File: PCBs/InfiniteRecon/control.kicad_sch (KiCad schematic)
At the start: 0 parts

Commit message: Finished Scem for the most part, awake me needs to look it over one more time
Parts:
- added C10, C11, C13, C15, C16: 0.1uF, PCM_JLCPCB:C_0402, symbol PCM_JLCPCB-Capacitors:0402,100nF
- added C12: 1uF, PCM_JLCPCB:C_0603, symbol PCM_JLCPCB-Capacitors:0603,1uF
- added C14: 22uF, PCM_JLCPCB:C_0805, symbol PCM_JLCPCB-Capacitors:0805,22uF
- added D6: WS2812B, LED_SMD:LED_WS2812B_PLCC4_5.0x5.0mm_P3.2mm, symbol LED:WS2812B
- added R14: 20kΩ, PCM_JLCPCB:R_0402, symbol Device:R_Small_US
- added R15, R28, R29, R30, R31: 10K, Resistor_SMD:R_01005_0402Metric, symbol Device:R_Small_US
- added R16: 100K, PCM_JLCPCB:R_0402, symbol Device:R_Small_US
- added R32, R33: 10K, Resistor_SMD:R_0603_1608Metric_Pad0.98x0.95mm_HandSolder, symbol Device:R_Small_US
- added S1: RESET, PCM_JLCPCB:SW-SMD_4P-L5.1-W5.1-P3.70-LS6.5-TL-2, symbol PCM_JLCPCB-Connectors_Buttons:Tactile Button, 160gf, 12V, 50mA, 5.1mm
- added S2: BOOT, PCM_JLCPCB:SW-SMD_4P-L5.1-W5.1-P3.70-LS6.5-TL-2, symbol PCM_JLCPCB-Connectors_Buttons:Tactile Button, 160gf, 12V, 50mA, 5.1mm
- added SIM1: 1040310811, Connector_Card:microSD_HC_Molex_104031-0811, symbol JLCImport:1040310811
- added U6: TPL5010DDCR, Package_TO_SOT_SMD:SOT-23-6, symbol JLCImport:TPL5010DDCR
- added U7: ESP32-S3-WROOM-1, RF_Module:ESP32-S3-WROOM-1, symbol RF_Module:ESP32-S3-WROOM-1
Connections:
- new net: C13.1, S2.2 (B), S2.4 (D), U7.27 (IO0)
- new net: R33.1, SIM1.8 (DAT1)
- new net: R14.2, U6.3 (DELAY/M_RST)
- new net: R32.1, SIM1.1 (DAT2)
- new net 3V3: C10.1, C14.1, C15.1, C16.1, D6.1 (VDD), R15.1, R16.1, R28.1, R29.1, U6.1 (VDD), U7.2 (3V3)
- new net 3V3_SW: R30.1, R31.1, R32.2, R33.2, SIM1.4 (VDD)
- new net 3V3_SW_EN: U7.34 (IO41)
- new net BATT_ALERT: U7.33 (IO40)
- new net CS: SIM1.2 (DAT3/CD), U7.7 (IO7)
- new net GND: C10.2, C11.2, C12.2, C13.2, C14.2, C15.2, C16.2, D6.3 (VSS), R14.1, S1.1 (A), S1.3 (C), S2.1 (A), S2.3 (C), SIM1.6 (VSS), SIM1.SH (SHIELD), U6.2 (GND), U7.1 (GND), U7.40 (GND), U7.41 (GND)
- new net MIC_THSEL: U7.32 (IO39)
- new net MIC_WAKE: U7.31 (IO38)
- new net MISO: SIM1.7 (DAT0), U7.17 (IO9)
- new net MOSI: SIM1.3 (CMD), U7.12 (IO8)
- new net NEOPIXEL: D6.4 (DIN), U7.25 (IO48)
- new net SCK: SIM1.5 (CLK), U7.18 (IO10)
- new net SCL_1: R28.2, U7.5 (IO5)
- new net SCL_SW: R30.2, U7.21 (IO13)
- new net SDA_1: R29.2, U7.4 (IO4)
- new net SDA_SW: R31.2, U7.20 (IO12)
- new net TDM_BCLK: U7.8 (IO15)
- new net TDM_FSYNC: U7.9 (IO16)
- new net TDM_SDOUT: U7.22 (IO14)
- new net USB_D+: U7.14 (USB_D+)
- new net USB_D-: U7.13 (USB_D-)
- new net WD_FEED: U6.4 (DONE), U7.38 (IO2)
- new net WD_RST: C11.1, C12.1, R15.2, R16.2, S1.2 (B), S1.4 (D), U6.6 (RSTn), U7.3 (EN)
- new net WD_WAKE: U6.5 (WAKE), U7.39 (IO1)
- no-connect marks 0 -> 17
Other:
- note added: "20K -> ~47s timer"
- note added: "ESP32S3 N8R8 Wroom-1"
- note added: "I2C Pullups"
- note added: "MicroSd Card"
- note added: "NeoPixel"
- note added: "Watchdog"

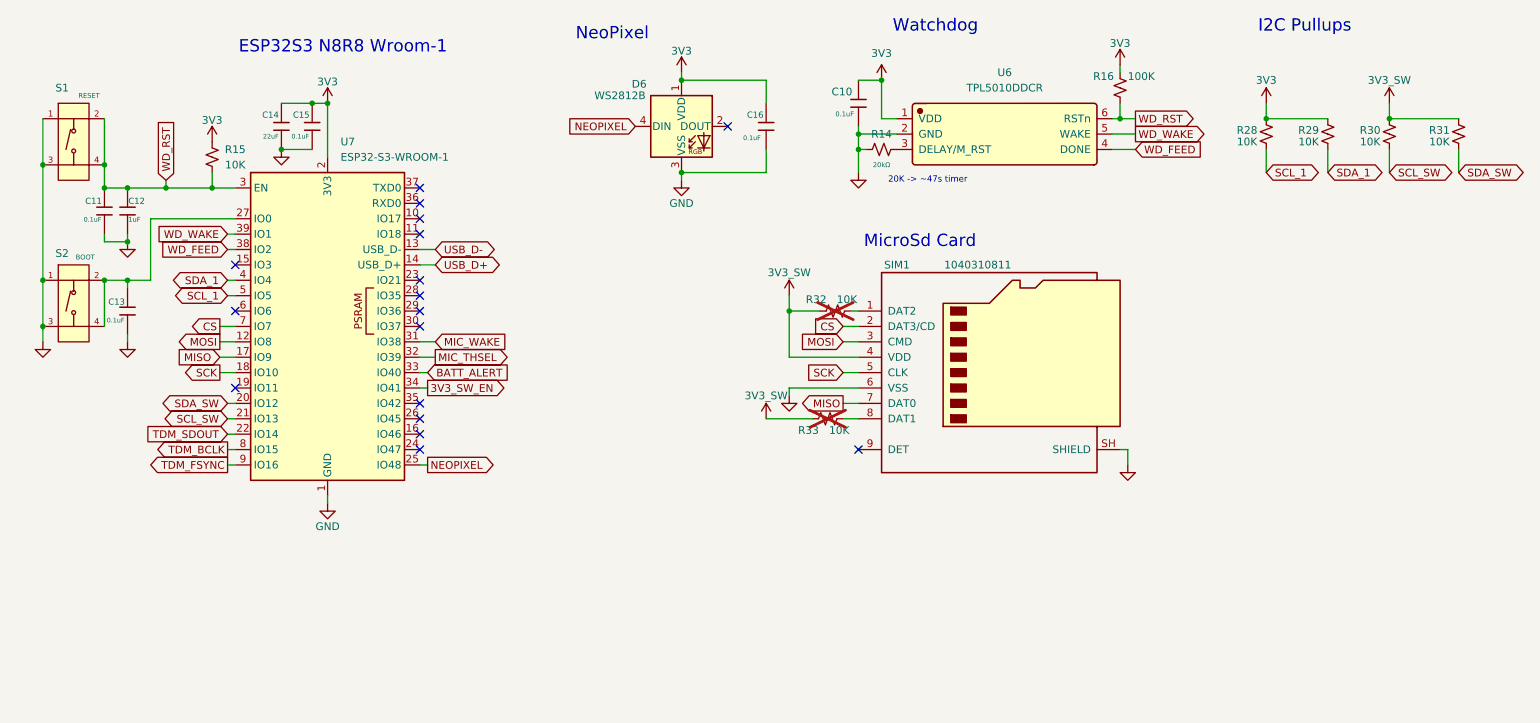
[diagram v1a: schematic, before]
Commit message: Fixed footprints and some not connected caps
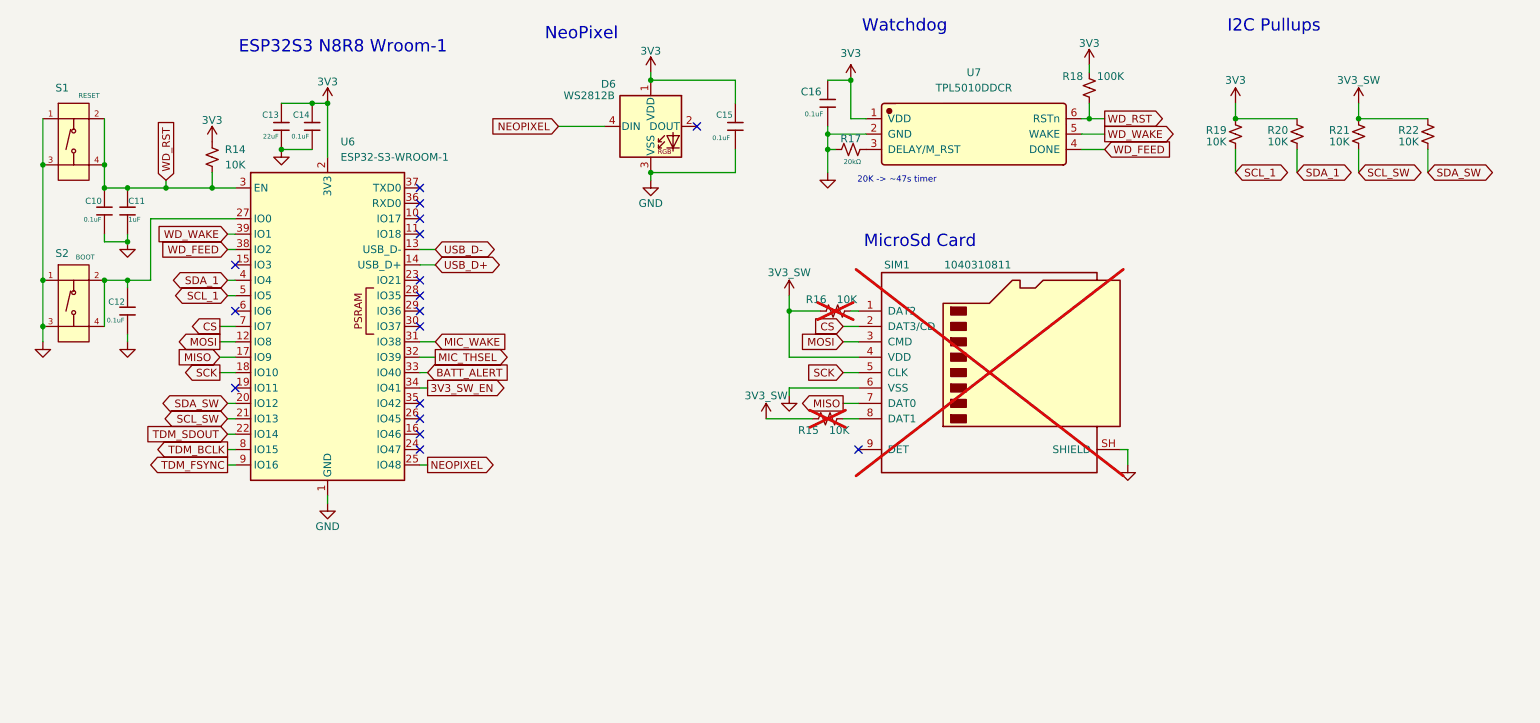
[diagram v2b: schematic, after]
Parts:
- R14: renamed from R15; footprint Resistor_SMD:R_01005_0402Metric -> Resistor_SMD:R_0402_1005Metric
- R19: renamed from R28; footprint Resistor_SMD:R_01005_0402Metric -> Resistor_SMD:R_0402_1005Metric
- R20: renamed from R29; footprint Resistor_SMD:R_01005_0402Metric -> Resistor_SMD:R_0402_1005Metric
- R21: renamed from R30; footprint Resistor_SMD:R_01005_0402Metric -> Resistor_SMD:R_0402_1005Metric
- R22: renamed from R31; footprint Resistor_SMD:R_01005_0402Metric -> Resistor_SMD:R_0402_1005Metric
- SIM1: now not fitted
- renumbered C11 to C10, C12 to C11, C13 to C12, C14 to C13, C15 to C14, C16 to C15, C10 to C16, R33 to R15, R32 to R16, R14 to R17, R16 to R18, U7 to U6, U6 to U7
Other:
- moved on the sheet: C15, C16, D6, R17, R18, R19, R20, R21, R22, U7

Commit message: Finished scem
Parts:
- added R34, R35, R39: 10K, Resistor_SMD:R_0603_1608Metric_Pad0.98x0.95mm_HandSolder, symbol Device:R_Small_US
- added R38: 100K, PCM_JLCPCB:R_0402, symbol Device:R_Small_US
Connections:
- net 3V3_SW: now also R15.1, R16.1, R34.1, R35.1, R39.1; no longer R15.2, R16.2
- net 3V3_SW_EN: now also R38.1
- net CS: now also R34.2
- net GND: now also R38.2
- net MISO: now also R35.2
- net MOSI: now also R39.2
- net at SIM1.8 (DAT1): now also R15.2; no longer R15.1
- net at SIM1.1 (DAT2): now also R16.2; no longer R16.1
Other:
- moved on the sheet: C10, C11, C12, C13, C14, C15, C16, D6, R14, R17, R18, R19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

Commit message: Reanotated
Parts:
- renumbered C10 to C16, C11 to C17, C12 to C18, C13 to C19, C14 to C20, C15 to C21, C16 to C22, R14 to R16, R38 to R17, R15 to R18, R35 to R19, R39 to R20, R34 to R21, R16 to R22, R17 to R23, R18 to R24, R19 to R25, R20 to R26, R21 to R27, R22 to R28, U6 to U7, U7 to U8

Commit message: lots of routing to be done
maybe its time to descope...
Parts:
- removed R24: 100K, PCM_JLCPCB:R_0402, symbol Device:R_Small_US
- removed S1: RESET, PCM_JLCPCB:SW-SMD_4P-L5.1-W5.1-P3.70-LS6.5-TL-2, symbol PCM_JLCPCB-Connectors_Buttons:Tactile Button, 160gf, 12V, 50mA, 5.1mm
- removed S2: BOOT, PCM_JLCPCB:SW-SMD_4P-L5.1-W5.1-P3.70-LS6.5-TL-2, symbol PCM_JLCPCB-Connectors_Buttons:Tactile Button, 160gf, 12V, 50mA, 5.1mm
- added J2: Conn_01x04_Pin, Connector_JST:JST_GH_SM04B-GHS-TB_1x04-1MP_P1.25mm_Horizontal, symbol Connector:Conn_01x04_Pin
- added S1, S2: Tactile Button, 160gf, PCM_JLCPCB:SW_TS-1088-AR02016, symbol PCM_JLCPCB-Connectors_Buttons:Tactile Button, 160gf, 12V, 50mA, 4.0mm
- R17, R23: footprint PCM_JLCPCB:R_0402 -> Resistor_SMD:R_0402_1005Metric
- renumbered R25 to R24, R26 to R25, R27 to R26, R28 to R27
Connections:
- net 3V3: now also J2.4 (Pin_4)
- net GND: now also J2.1 (Pin_1), S1.1 (A), S2.1 (A)
- net WD_RST: now also S1.2 (B)
- net at C18.1, U7.27 (IO0): now also S2.2 (B)
- net TX: now reaches U7.36 (RXD0)
- net TX: now also J2.3 (Pin_3)
- net RX: now reaches U7.37 (TXD0)
- net RX: now also J2.2 (Pin_2)
- no-connect marks 17 -> 15
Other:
- note added: "UART"

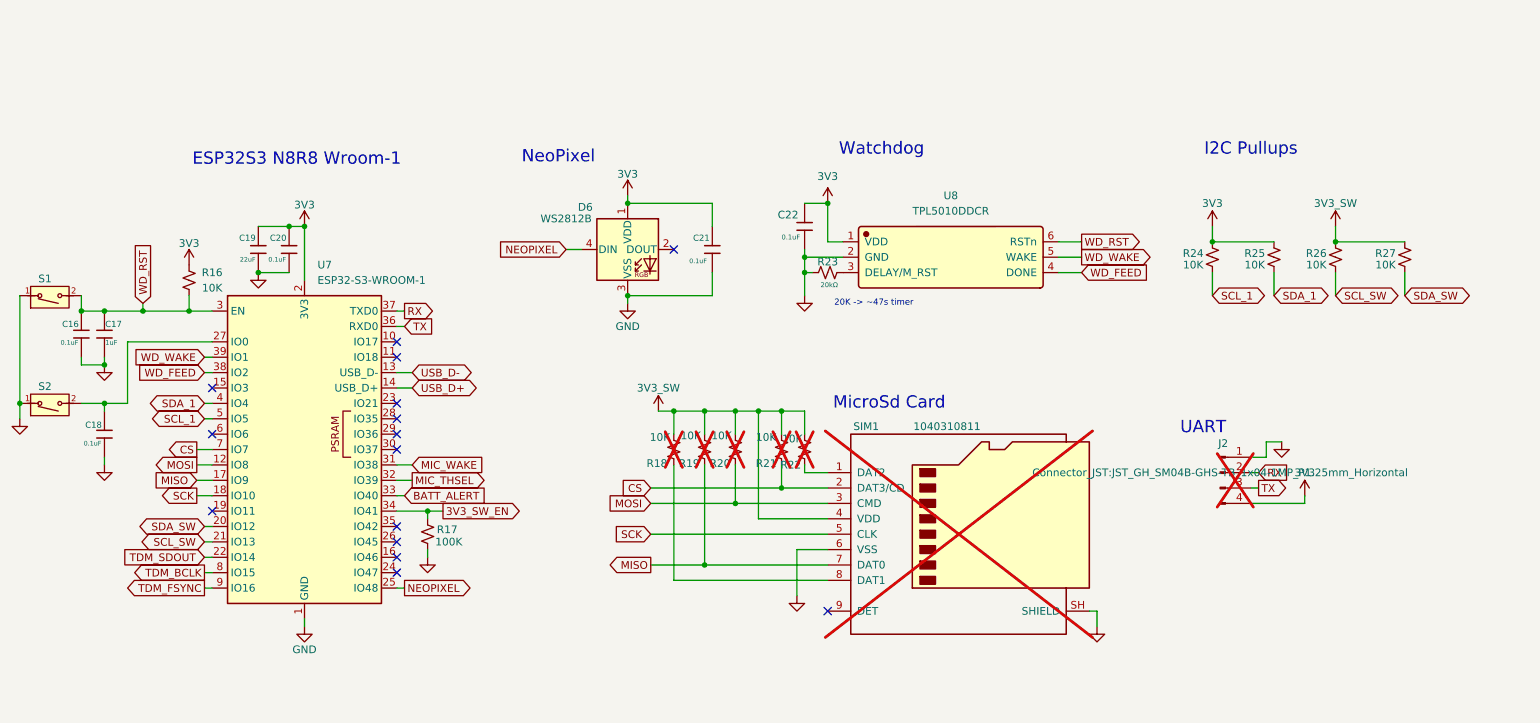
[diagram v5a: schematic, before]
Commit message: Layout more or less done. Still missing i2c pullups and need to redo pinout
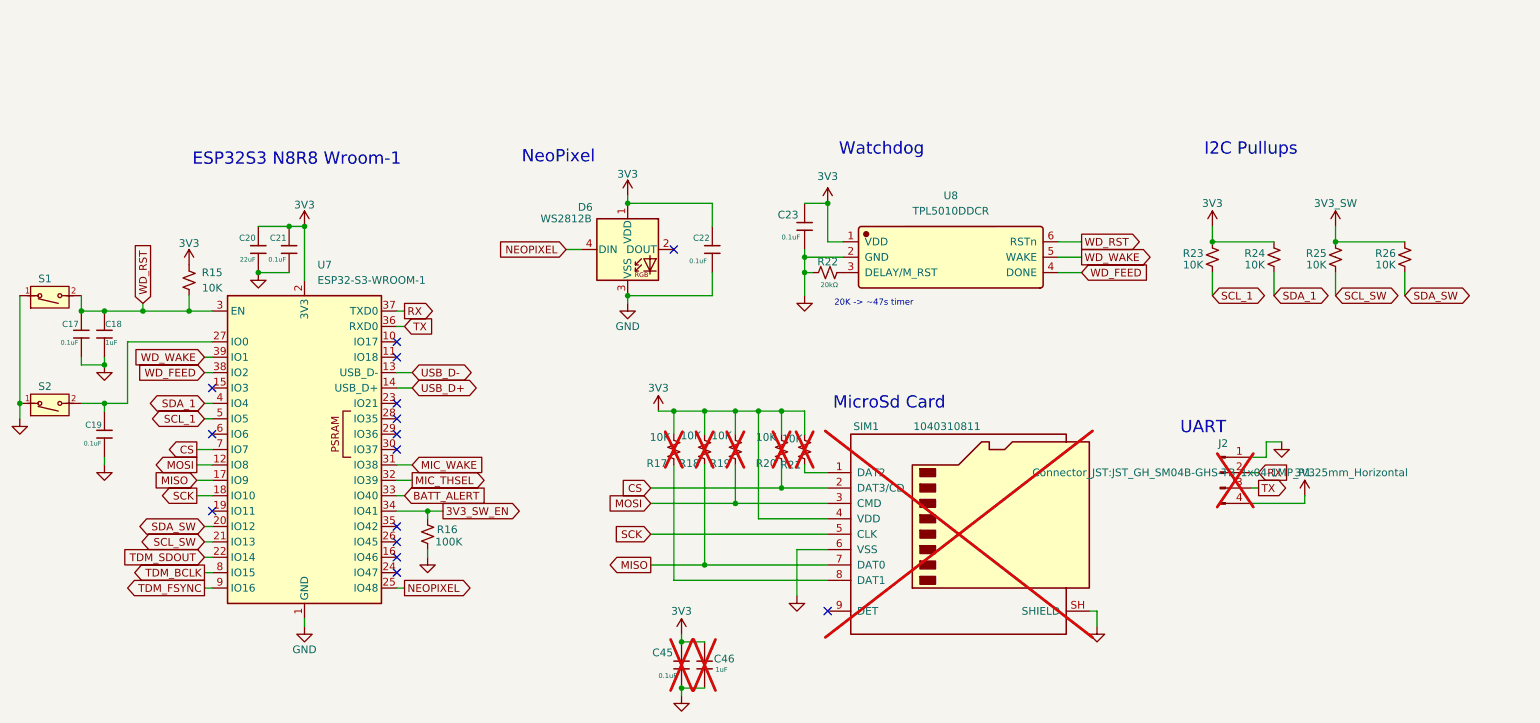
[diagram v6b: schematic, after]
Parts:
- added C45: 0.1uF, PCM_JLCPCB:C_0402, symbol PCM_JLCPCB-Capacitors:0402,100nF
- added C46: 1uF, PCM_JLCPCB:C_0603, symbol PCM_JLCPCB-Capacitors:0603,1uF
- renumbered C16 to C17, C17 to C18, C18 to C19, C19 to C20, C20 to C21, C21 to C22, C22 to C23, R16 to R15, R17 to R16, R18 to R17, R19 to R18, R20 to R19, R21 to R20, R22 to R21, R23 to R22, R24 to R23, R25 to R24, R26 to R25, R27 to R26
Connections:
- net 3V3: now also R17.1, R18.1, R19.1, R20.1, R21.1, SIM1.4 (VDD), C45.1, C46.1
- net 3V3_SW: no longer R17.1, R18.1, R19.1, R20.1, R21.1, SIM1.4 (VDD)
- net GND: now also C45.2, C46.2
